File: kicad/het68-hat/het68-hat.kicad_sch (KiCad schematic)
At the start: 87 parts, among them J1 MIC1, J10 PWR, J11 PZ1, J12 PZ2, J13 PZ3, J14 PZ4, J17 UART, J2 MIC2, J3 MIC3, J4 MIC4, J5 MIC5, J6 MIC6, U1 Pico_Plus_2, U2 SN74LVC8T245, U3 SN74LVC8T245, U4 SN74LVC8T245, U5 AP2112K-1.8, U6 DRV8837, U7 DPS310, U8 SHT40, U9 INA3221

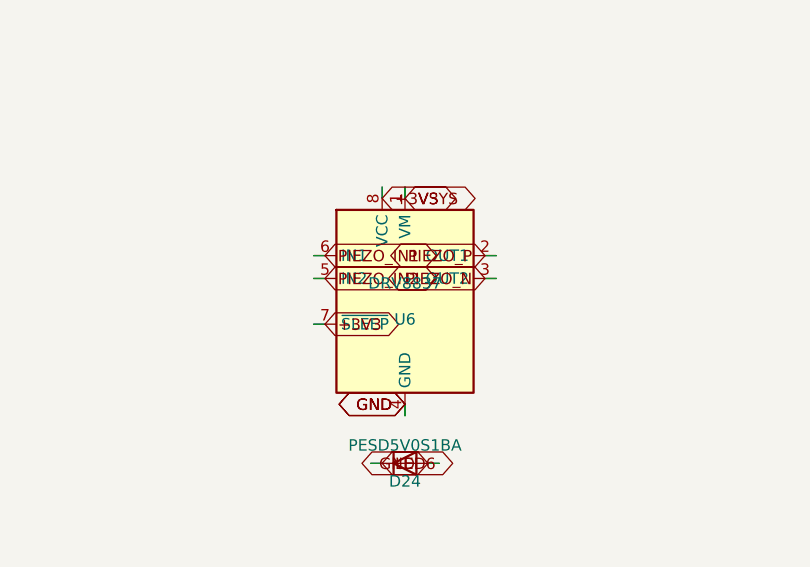
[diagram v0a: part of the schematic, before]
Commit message: Switch the boards to two layers and specify the power sources.
The HAT is no longer four-layer and the gerbers match that stackup. The power board now names the clamp CT, solar MPPT, 21700 cell and 5 V output; those charger parts are not drawn in KiCad yet.

Co-authored-by: Cursor <cursoragent@cursor.com>
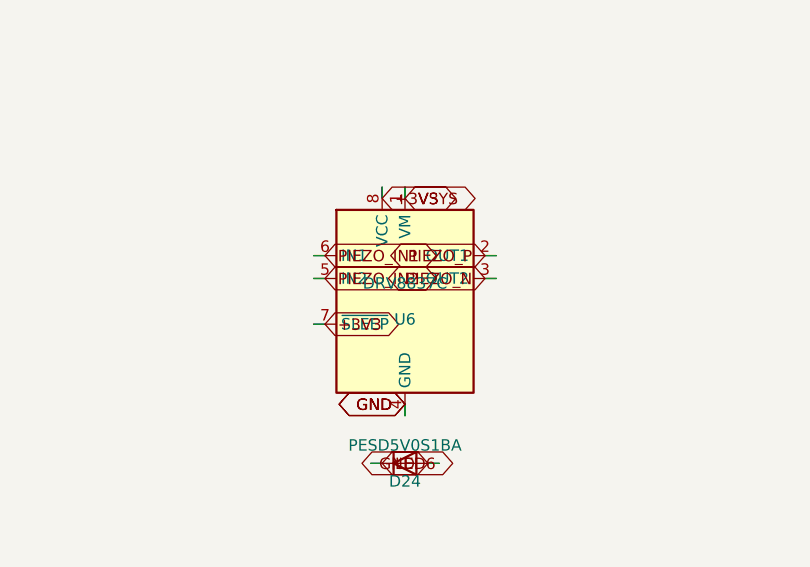
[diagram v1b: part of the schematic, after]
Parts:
- U6: value DRV8837 -> DRV8837C; MPN DRV8837DSGR -> DRV8837CDSGR
